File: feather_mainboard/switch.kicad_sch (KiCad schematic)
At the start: 1 part

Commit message: changed footprints location to match the new folder. TODO: check if the path is working on another computer
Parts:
- S1: footprint footprints:450406020024 -> Custom footprints:450406020024
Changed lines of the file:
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@@
 			)
 		)
-		(property "Footprint" "footprints:450406020024"
+		(property "Footprint" "Custom footprints:450406020024"
 			(at 143.51 101.6 0)
 			(effects

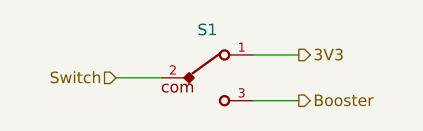
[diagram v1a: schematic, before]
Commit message: added daughter board
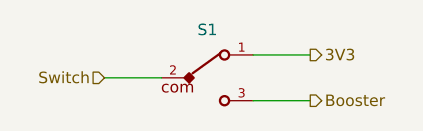
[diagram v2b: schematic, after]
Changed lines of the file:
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@@
 	(wire
 		(pts
-			(xy 148.59 99.06) (xy 153.67 99.06)
+			(xy 148.59 99.06) (xy 154.94 99.06)
 		)
 		(stroke
@@
 	(wire
 		(pts
-			(xy 133.35 101.6) (xy 138.43 101.6)
+			(xy 132.08 101.6) (xy 138.43 101.6)
 		)
 		(stroke
@@
 	(wire
 		(pts
-			(xy 148.59 104.14) (xy 153.67 104.14)
+			(xy 148.59 104.14) (xy 154.94 104.14)
 		)
 		(stroke
@@
 	(hierarchical_label "Booster"
 		(shape output)
-		(at 153.67 104.14 0)
+		(at 154.94 104.14 0)
 		(fields_autoplaced yes)
 		(effects
@@
 	(hierarchical_label "3V3"
 		(shape output)
-		(at 153.67 99.06 0)
+		(at 154.94 99.06 0)
 		(fields_autoplaced yes)
 		(effects
@@
 	(hierarchical_label "Switch"
 		(shape input)
-		(at 133.35 101.6 180)
+		(at 132.08 101.6 180)
 		(fields_autoplaced yes)
 		(effects

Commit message: finished mainboard design, need to do the routing
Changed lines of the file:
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@@
 	)
 	(hierarchical_label "Booster"
-		(shape output)
+		(shape bidirectional)
 		(at 154.94 104.14 0)
 		(fields_autoplaced yes)
@@
 	)
 	(hierarchical_label "3V3"
-		(shape output)
+		(shape bidirectional)
 		(at 154.94 99.06 0)
 		(fields_autoplaced yes)
@@
 	)
 	(hierarchical_label "Switch"
-		(shape input)
+		(shape bidirectional)
 		(at 132.08 101.6 180)
 		(fields_autoplaced yes)
